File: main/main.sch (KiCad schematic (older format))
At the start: 0 parts

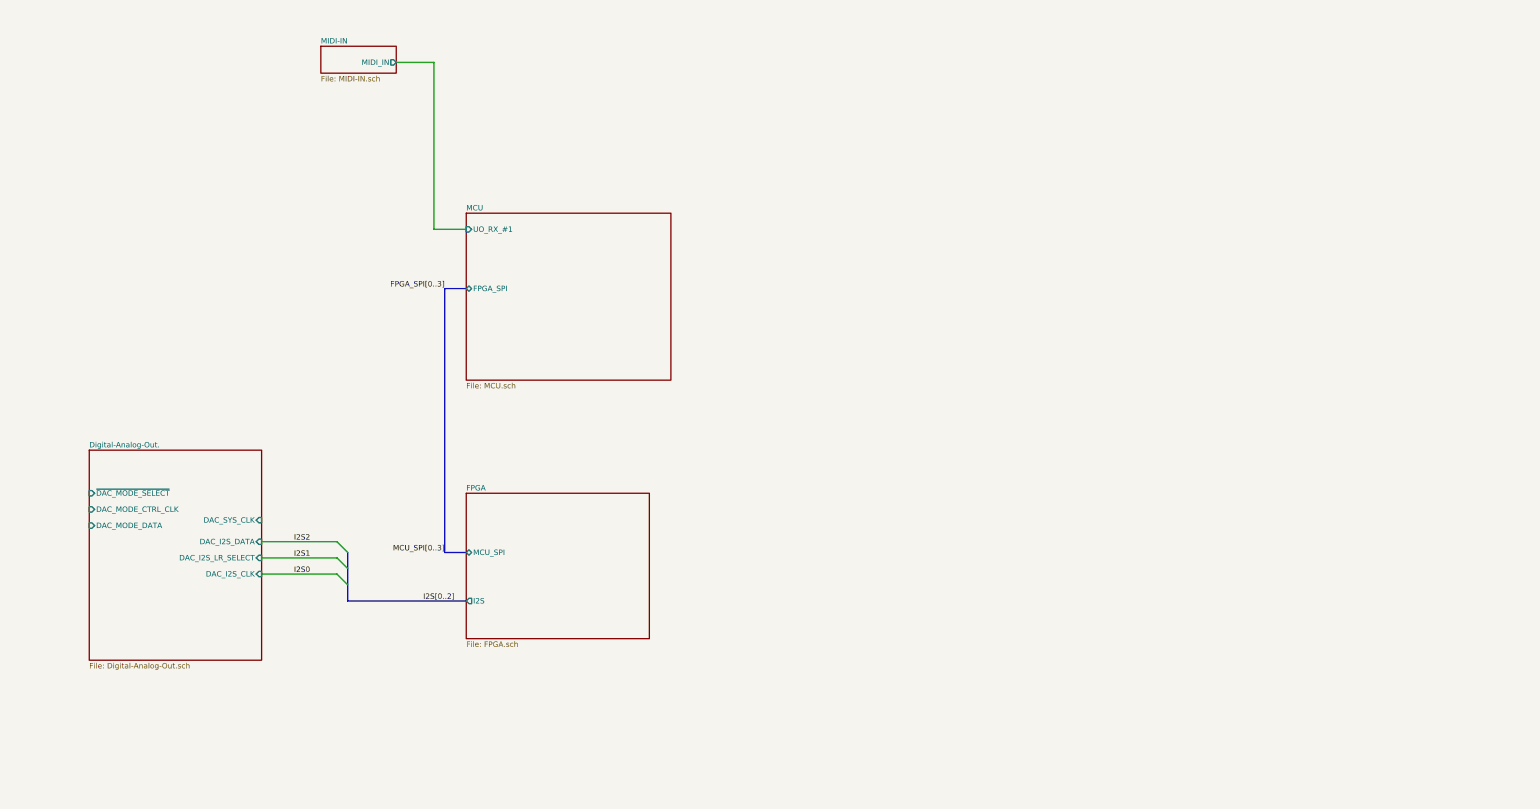
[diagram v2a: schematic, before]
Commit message: Simplify the top sheet, put bus connection inside the sheets
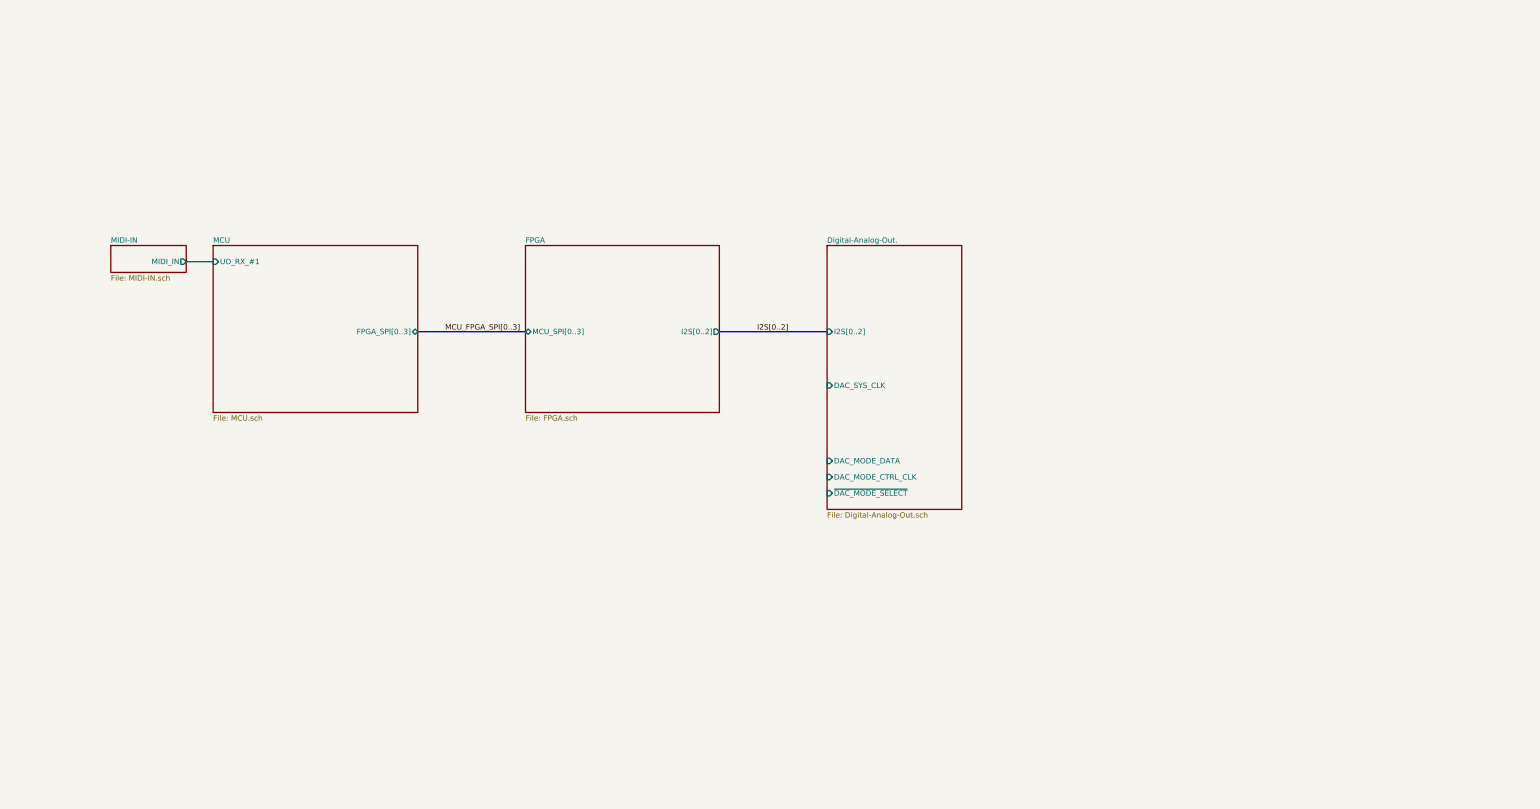
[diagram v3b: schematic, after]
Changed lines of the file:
@@
 $EndDescr
 $Sheet
-S 3450 700  700  250
+S 1500 2550 700  250
 U 613F97F2
 F0 "MIDI-IN" 50
 F1 "MIDI-IN.sch" 50
-F2 "MIDI_IN" O R 4150 850 50
+F2 "MIDI_IN" O R 2200 2700 50
 $EndSheet
-Wire Wire Line
-	4150 850  4500 850
-Wire Wire Line
-	4500 850  4500 2400
-Wire Wire Line
-	4500 2400 4800 2400
 $Sheet
-S 1300 4450 1600 1950
+S 8150 2550 1250 2450
 U 61417224
 F0 "Digital-Analog-Out." 50
 F1 "Digital-Analog-Out.sch" 50
-F2 "~DAC_MODE_SELECT" I L 1300 4850 50
-F3 "DAC_MODE_CTRL_CLK" I L 1300 5000 50
-F4 "DAC_MODE_DATA" I L 1300 5150 50
-F5 "DAC_SYS_CLK" I R 2900 5100 50
-F6 "DAC_I2S_DATA" I R 2900 5300 50
-F7 "DAC_I2S_CLK" I R 2900 5600 50
-F8 "DAC_I2S_LR_SELECT" I R 2900 5450 50
+F2 "~DAC_MODE_SELECT" I L 8150 4850 50
+F3 "DAC_MODE_CTRL_CLK" I L 8150 4700 50
+F4 "DAC_MODE_DATA" I L 8150 4550 50
+F5 "DAC_SYS_CLK" I L 8150 3850 50
+F6 "I2S[0..2]" I L 8150 3350 50
 $EndSheet
-Entry Wire Line
-	3600 5300 3700 5400
-Entry Wire Line
-	3600 5450 3700 5550
-Entry Wire Line
-	3600 5600 3700 5700
-Wire Wire Line
-	2900 5300 3600 5300
-Wire Wire Line
-	2900 5450 3600 5450
-Wire Wire Line
-	2900 5600 3600 5600
-Text Label 4400 5850 0    50   ~ 0
+Text Label 7500 3350 0    50   ~ 0
 I2S[0..2]
-Text Label 3200 5300 0    50   ~ 0
-I2S2
-Text Label 3200 5450 0    50   ~ 0
-I2S1
-Text Label 3200 5600 0    50   ~ 0
-I2S0
-Wire Bus Line
-	3700 5850 4800 5850
 $Sheet
-S 4800 4850 1700 1350
+S 5350 2550 1800 1550
 U 613F0EEF
 F0 "FPGA" 50
 F1 "FPGA.sch" 50
-F2 "I2S" O L 4800 5850 50
-F3 "MCU_SPI" B L 4800 5400 50
+F2 "I2S[0..2]" O R 7150 3350 50
+F3 "MCU_SPI[0..3]" B L 5350 3350 50
 $EndSheet
-Wire Bus Line
-	4800 2950 4600 2950
-Wire Bus Line
-	4600 2950 4600 5400
-Wire Bus Line
-	4600 5400 4800 5400
-Text Label 4600 5400 2    50   ~ 0
-MCU_SPI[0..3]
-Text Label 4600 2950 2    50   ~ 0
-FPGA_SPI[0..3]
+Text Label 5300 3350 2    50   ~ 0
+MCU_FPGA_SPI[0..3]
 $Sheet
-S 4800 2250 1900 1550
+S 2450 2550 1900 1550
 U 6139E7E0
 F0 "MCU" 50
 F1 "MCU.sch" 50
-F2 "UO_RX_#1" I L 4800 2400 50
-F3 "FPGA_SPI" B L 4800 2950 50
+F2 "UO_RX_#1" I L 2450 2700 50
+F3 "FPGA_SPI[0..3]" B R 4350 3350 50
 $EndSheet
+Wire Wire Line
+	2200 2700 2450 2700
 Wire Bus Line
-	3700 5400 3700 5850
+	4350 3350 5350 3350
+Wire Bus Line
+	7150 3350 8150 3350
 $EndSCHEMATC

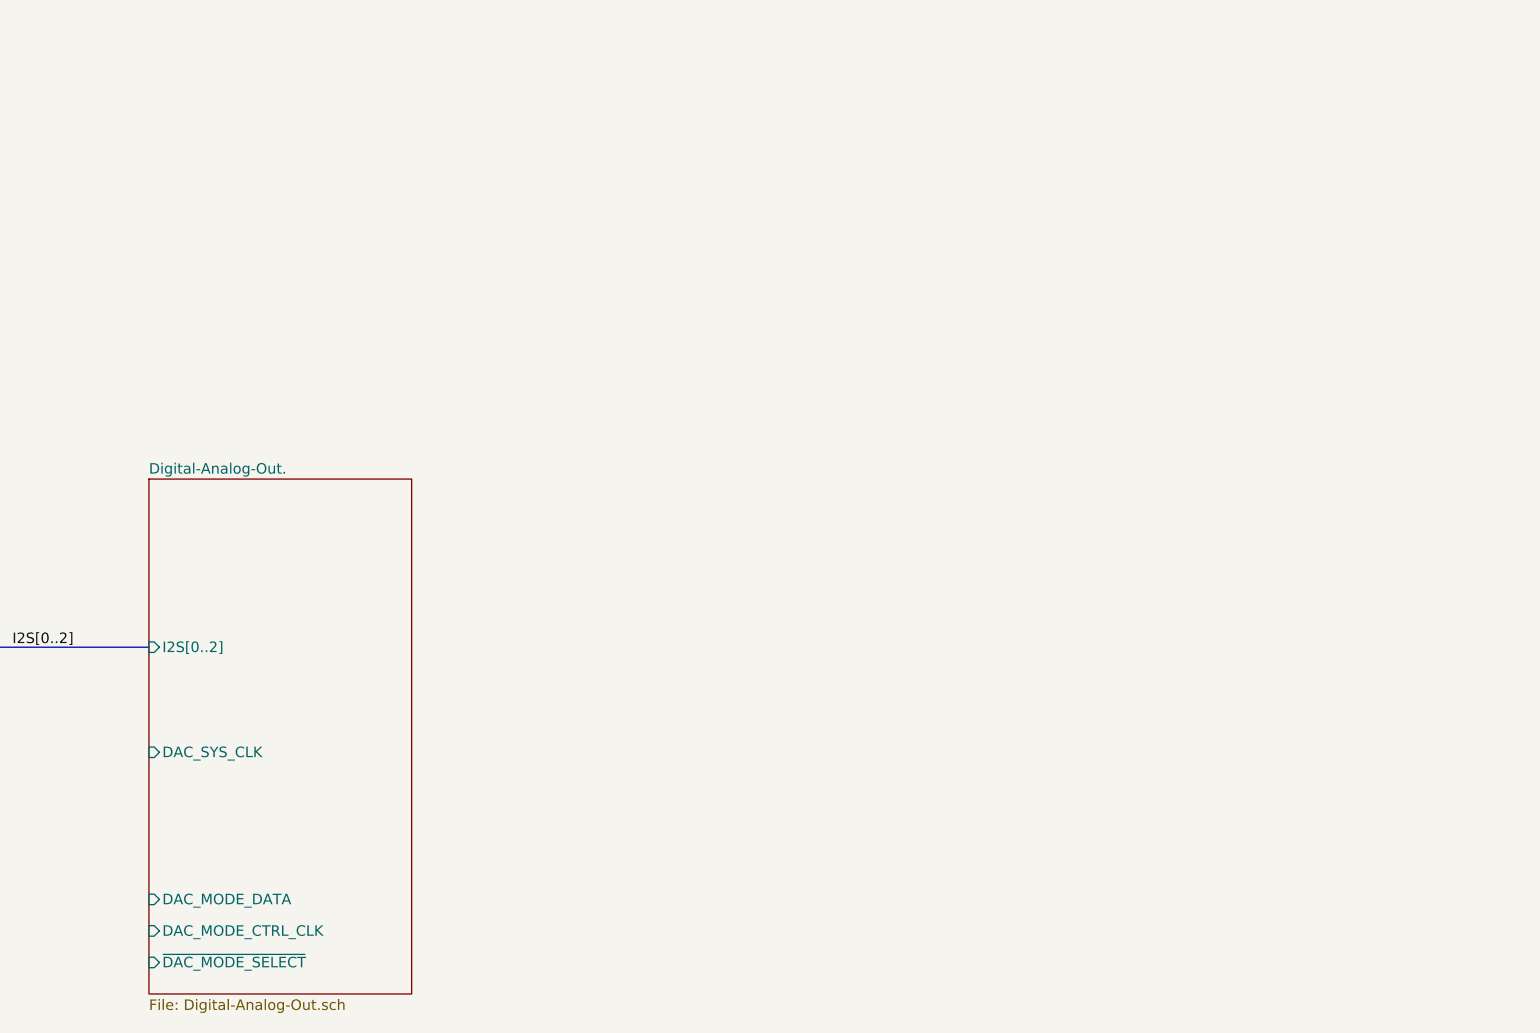
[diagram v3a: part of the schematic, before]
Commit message: Setup FPGA power connections, connect FPGA flash
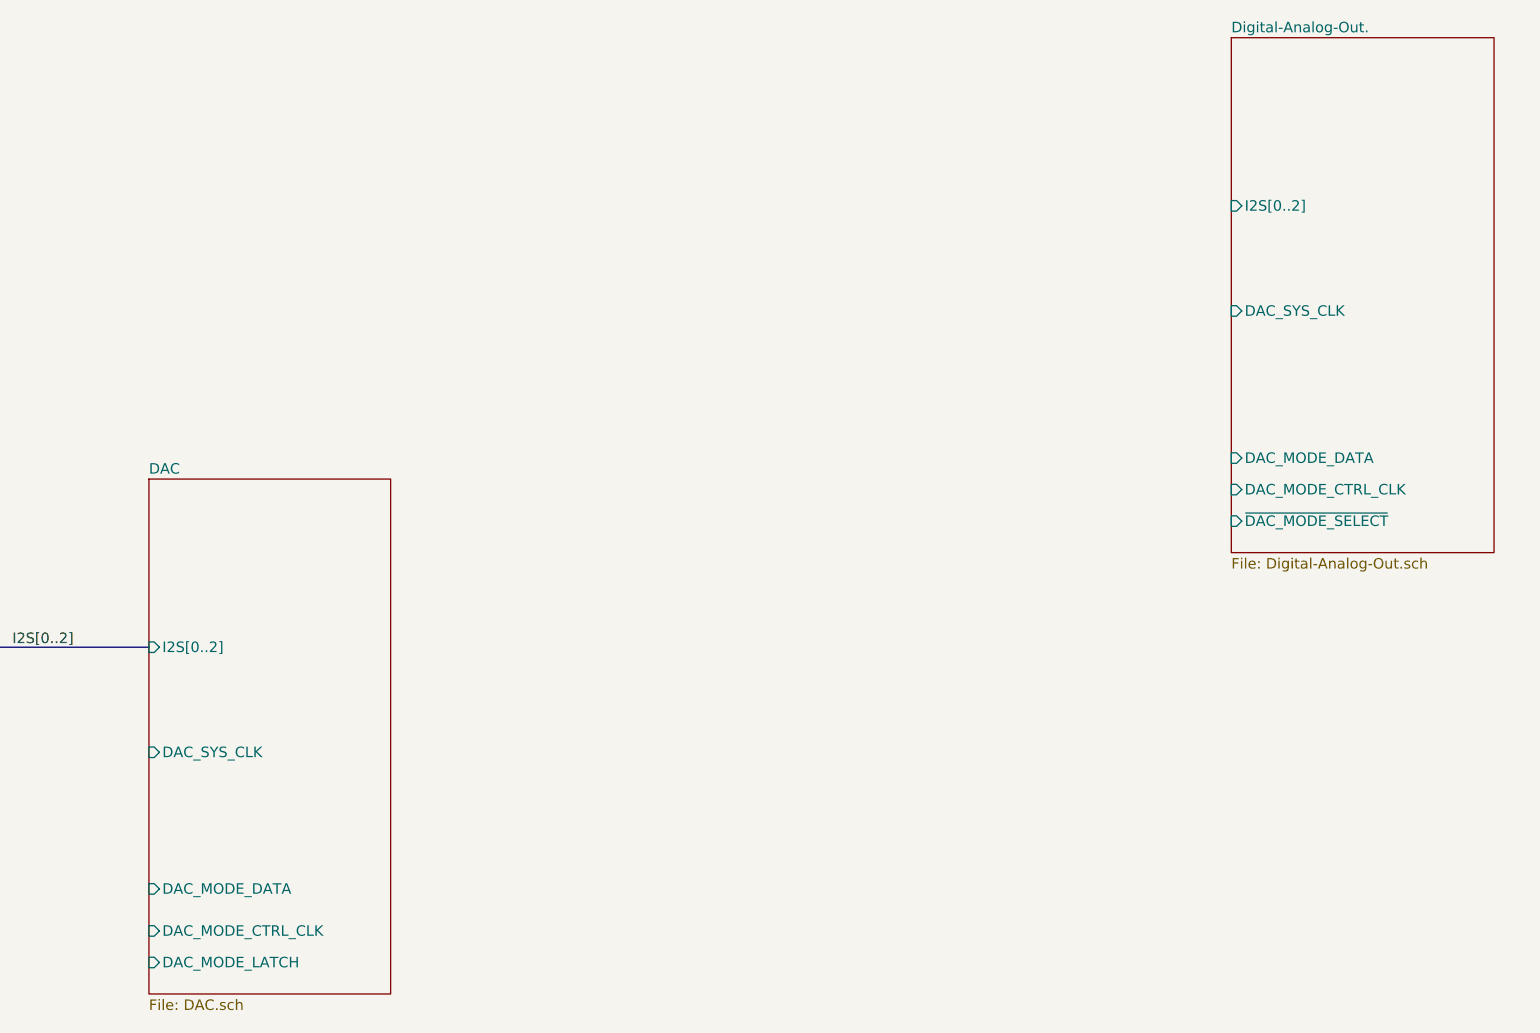
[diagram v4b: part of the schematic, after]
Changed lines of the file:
@@
 $Descr A4 11693 8268
 encoding utf-8
-Sheet 1 5
+Sheet 1 6
 Title "Synthesizer"
 Date "2021-09-06"
@@
 $EndSheet
 $Sheet
-S 8150 2550 1250 2450
+S 13300 450  1250 2450
 U 61417224
 F0 "Digital-Analog-Out." 50
 F1 "Digital-Analog-Out.sch" 50
-F2 "~DAC_MODE_SELECT" I L 8150 4850 50
-F3 "DAC_MODE_CTRL_CLK" I L 8150 4700 50
-F4 "DAC_MODE_DATA" I L 8150 4550 50
-F5 "DAC_SYS_CLK" I L 8150 3850 50
-F6 "I2S[0..2]" I L 8150 3350 50
+F2 "~DAC_MODE_SELECT" I L 13300 2750 50
+F3 "DAC_MODE_CTRL_CLK" I L 13300 2600 50
+F4 "DAC_MODE_DATA" I L 13300 2450 50
+F5 "DAC_SYS_CLK" I L 13300 1750 50
+F6 "I2S[0..2]" I L 13300 1250 50
 $EndSheet
 Text Label 7500 3350 0    50   ~ 0
@@
 Wire Bus Line
 	7150 3350 8150 3350
+$Sheet
+S 8150 2550 1150 2450
+U 61496F7B
+F0 "DAC" 50
+F1 "DAC.sch" 50
+F2 "I2S[0..2]" I L 8150 3350 50
+F3 "DAC_SYS_CLK" I L 8150 3850 50
+F4 "DAC_MODE_DATA" I L 8150 4500 50
+F5 "DAC_MODE_CTRL_CLK" I L 8150 4700 50
+F6 "DAC_MODE_LATCH" I L 8150 4850 50
+$EndSheet
 $EndSCHEMATC

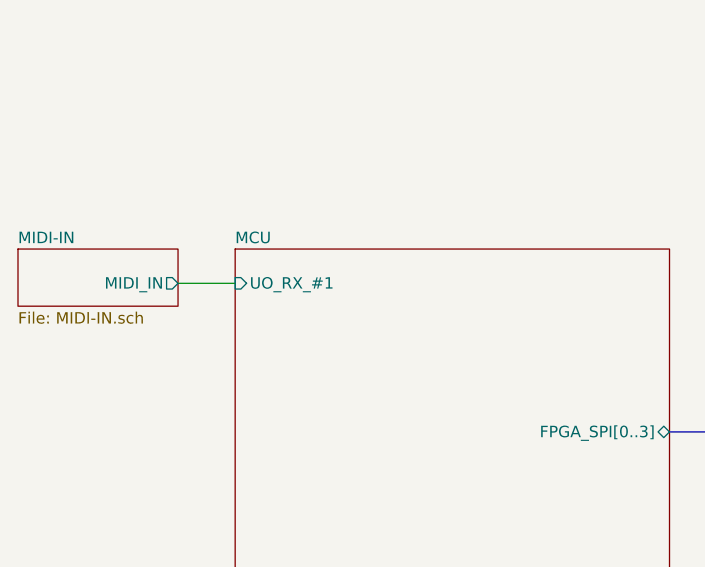
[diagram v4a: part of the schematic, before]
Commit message: Finish (?) setting up FPGA as in the slides
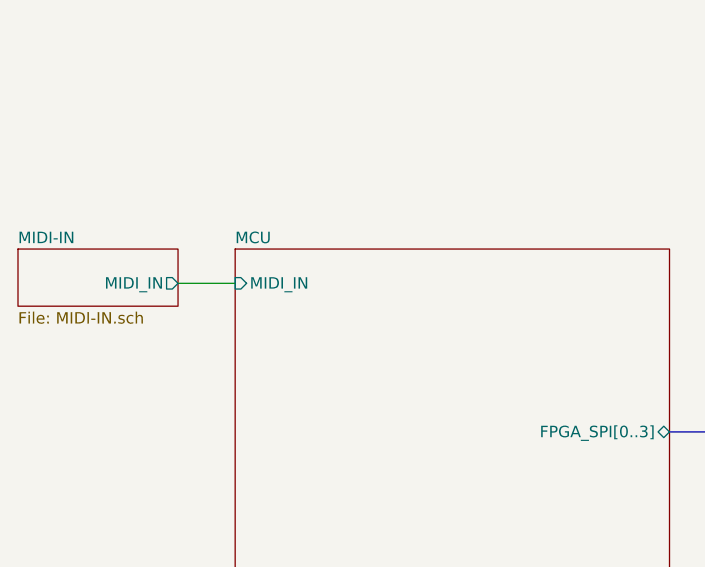
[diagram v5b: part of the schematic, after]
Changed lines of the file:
@@
 F0 "MCU" 50
 F1 "MCU.sch" 50
-F2 "UO_RX_#1" I L 2450 2700 50
+F2 "MIDI_IN" I L 2450 2700 50
 F3 "FPGA_SPI[0..3]" B R 4350 3350 50
 $EndSheet
